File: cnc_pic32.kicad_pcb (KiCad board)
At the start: 4 copper layers, 206.5 x 158.5 mm, 111 parts, among them J1 icd, J13 mrf24j40_tp, J14 mrf24j40_tp, J18 USB_B_Mini, J2 ST7789 oled 128x64, J20 pololu, J21 pololu, J22 pololu, J23 conector oled ST1306 128x32, J24 pololu, J25 pololu, J5 USB_B_Mini, Q1 2N7002, SW2 up, U1 PIC32MX795F512L-80x-PF, U2 FT232BM, U3 LM1117DT-3.3, U4 MRF24J40MA, U5 LM1117DT-3.3, Y2 6MHZ

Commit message: Fix Y1/J17 footprints, update PCB and schematics
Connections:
- U1 pad 21: unconnected-(U1-RB4-Pad21) -> /MCU/RB4
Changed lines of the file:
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@@
 		)
 		(embedded_fonts no)
-		(model "${KICAD6_3DMODEL_DIR}/Resistor_SMD.3dshapes/R_0805_2012Metric.wrl"
+		(model "${KICAD10_3DMODEL_DIR}/Resistor_SMD.3dshapes/R_0805_2012Metric.step"
 			(offset
 				(xyz 0 0 0)
@@
 		)
 		(embedded_fonts no)
-		(model "${KICAD6_3DMODEL_DIR}/Capacitor_SMD.3dshapes/C_0805_2012Metric.wrl"
+		(model "${KICAD10_3DMODEL_DIR}/Capacitor_SMD.3dshapes/C_0805_2012Metric.step"
 			(offset
 				(xyz 0 0 0)
@@
 		)
 		(embedded_fonts no)
-		(model "${KICAD6_3DMODEL_DIR}/Connector_PinHeader_2.54mm.3dshapes/PinHeader_1x06_P2.54mm_Horizontal.wrl"
+		(model "${KICAD10_3DMODEL_DIR}/Connector_PinHeader_2.54mm.3dshapes/PinHeader_1x06_P2.54mm_Horizontal.step"
 			(offset
 				(xyz 0 0 0)
@@
 		)
 		(embedded_fonts no)
-		(model "${KICAD6_3DMODEL_DIR}/Capacitor_SMD.3dshapes/C_0805_2012Metric.wrl"
+		(model "${KICAD10_3DMODEL_DIR}/Capacitor_SMD.3dshapes/C_0805_2012Metric.step"
 			(offset
 				(xyz 0 0 0)
@@
 		)
 		(embedded_fonts no)
-		(model "${KICAD6_3DMODEL_DIR}/Resistor_SMD.3dshapes/R_0805_2012Metric.wrl"
+		(model "${KICAD10_3DMODEL_DIR}/Resistor_SMD.3dshapes/R_0805_2012Metric.step"
 			(offset
 				(xyz 0 0 0)
@@
 		)
 		(embedded_fonts no)
-		(model "${KICAD6_3DMODEL_DIR}/Connector_PinHeader_2.54mm.3dshapes/PinHeader_1x06_P2.54mm_Vertical.wrl"
+		(model "${KICAD10_3DMODEL_DIR}/Connector_PinHeader_2.54mm.3dshapes/PinHeader_1x06_P2.54mm_Vertical.step"
 			(offset
 				(xyz 0 0 0)
@@
 		)
 		(embedded_fonts no)
-		(model "${KICAD6_3DMODEL_DIR}/Capacitor_SMD.3dshapes/C_0805_2012Metric.wrl"
+		(model "${KICAD10_3DMODEL_DIR}/Capacitor_SMD.3dshapes/C_0805_2012Metric.step"
 			(offset
 				(xyz 0 0 0)
@@
 		)
 		(embedded_fonts no)
-		(model "${KICAD6_3DMODEL_DIR}/Resistor_SMD.3dshapes/R_0805_2012Metric.wrl"
+		(model "${KICAD10_3DMODEL_DIR}/Resistor_SMD.3dshapes/R_0805_2012Metric.step"
 			(offset
 				(xyz 0 0 0)
@@
 		)
 		(embedded_fonts no)
-		(model "${KICAD6_3DMODEL_DIR}/Capacitor_SMD.3dshapes/C_0805_2012Metric.wrl"
+		(model "${KICAD10_3DMODEL_DIR}/Capacitor_SMD.3dshapes/C_0805_2012Metric.step"
 			(offset
 				(xyz 0 0 0)
@@
 		)
 		(embedded_fonts no)
-		(model "${KICAD6_3DMODEL_DIR}/Resistor_SMD.3dshapes/R_0805_2012Metric.wrl"
+		(model "${KICAD10_3DMODEL_DIR}/Resistor_SMD.3dshapes/R_0805_2012Metric.step"
 			(offset
 				(xyz 0 0 0)
@@
 		)
 		(embedded_fonts no)
-		(model "${KICAD6_3DMODEL_DIR}/Connector_PinHeader_2.54mm.3dshapes/PinHeader_1x06_P2.54mm_Vertical.wrl"
+		(model "${KICAD10_3DMODEL_DIR}/Connector_PinHeader_2.54mm.3dshapes/PinHeader_1x06_P2.54mm_Vertical.step"
 			(offset
 				(xyz 0 0 0)
@@
 		)
 		(embedded_fonts no)
-		(model "${KICAD6_3DMODEL_DIR}/Connector_PinHeader_2.54mm.3dshapes/PinHeader_1x06_P2.54mm_Vertical.wrl"
+		(model "${KICAD10_3DMODEL_DIR}/Connector_PinHeader_2.54mm.3dshapes/PinHeader_1x06_P2.54mm_Vertical.step"
 			(offset
 				(xyz 0 0 0)
@@
 		)
 		(embedded_fonts no)
-		(model "${KICAD6_3DMODEL_DIR}/Resistor_SMD.3dshapes/R_0805_2012Metric.wrl"
+		(model "${KICAD10_3DMODEL_DIR}/Resistor_SMD.3dshapes/R_0805_2012Metric.step"
 			(offset
 				(xyz 0 0 0)
@@
 		)
 		(embedded_fonts no)
-		(model "${KICAD6_3DMODEL_DIR}/Resistor_SMD.3dshapes/R_0805_2012Metric.wrl"
+		(model "${KICAD10_3DMODEL_DIR}/Resistor_SMD.3dshapes/R_0805_2012Metric.step"
 			(offset
 				(xyz 0 0 0)
@@
 		)
 		(embedded_fonts no)
-		(model "${KICAD6_3DMODEL_DIR}/Resistor_SMD.3dshapes/R_0805_2012Metric.wrl"
+		(model "${KICAD10_3DMODEL_DIR}/Resistor_SMD.3dshapes/R_0805_2012Metric.step"
 			(offset
 				(xyz 0 0 0)
@@
 			)
 		)
-		(attr smd dnp)
+		(attr smd)
 		(duplicate_pad_numbers_are_jumpers no)
 		(fp_line
@@
 		)
 		(embedded_fonts no)
-		(model "${KICAD6_3DMODEL_DIR}/Resistor_SMD.3dshapes/R_0805_2012Metric.wrl"
+		(model "${KICAD10_3DMODEL_DIR}/Resistor_SMD.3dshapes/R_0805_2012Metric.step"
 			(offset
 				(xyz 0 0 0)
@@
 		)
 		(embedded_fonts no)
-		(model "${KICAD6_3DMODEL_DIR}/Display.3dshapes/Adafruit_SSD1306.wrl"
+		(model "${KICAD10_3DMODEL_DIR}/Display.3dshapes/Adafruit_SSD1306.step"
 			(offset
 				(xyz 0 0 0)
@@
 		)
 		(embedded_fonts no)
-		(model "${KICAD6_3DMODEL_DIR}/Resistor_SMD.3dshapes/R_0805_2012Metric.wrl"
+		(model "${KICAD10_3DMODEL_DIR}/Resistor_SMD.3dshapes/R_0805_2012Metric.step"
 			(offset
 				(xyz 0 0 0)
@@
 		)
 		(embedded_fonts no)
-		(model "${KICAD6_3DMODEL_DIR}/Resistor_SMD.3dshapes/R_0805_2012Metric.wrl"
+		(model "${KICAD10_3DMODEL_DIR}/Resistor_SMD.3dshapes/R_0805_2012Metric.step"
 			(offset
 				(xyz 0 0 0)
@@
 		)
 		(embedded_fonts no)
-		(model "${KICAD6_3DMODEL_DIR}/Connector_PinHeader_2.54mm.3dshapes/PinHeader_1x06_P2.54mm_Vertical.wrl"
+		(model "${KICAD10_3DMODEL_DIR}/Connector_PinHeader_2.54mm.3dshapes/PinHeader_1x06_P2.54mm_Vertical.step"
 			(offset
 				(xyz 0 0 0)
@@
 		)
 		(embedded_fonts no)
-		(model "${KICAD6_3DMODEL_DIR}/Capacitor_SMD.3dshapes/C_0805_2012Metric.wrl"
+		(model "${KICAD10_3DMODEL_DIR}/Capacitor_SMD.3dshapes/C_0805_2012Metric.step"
 			(offset
 				(xyz 0 0 0)
@@
 		)
 		(embedded_fonts no)
-		(model "${KICAD6_3DMODEL_DIR}/Resistor_SMD.3dshapes/R_0805_2012Metric.wrl"
+		(model "${KICAD10_3DMODEL_DIR}/Resistor_SMD.3dshapes/R_0805_2012Metric.step"
 			(offset
 				(xyz 0 0 0)
@@
 		)
 		(embedded_fonts no)
-		(model "${KICAD6_3DMODEL_DIR}/Capacitor_SMD.3dshapes/C_0805_2012Metric.wrl"
+		(model "${KICAD10_3DMODEL_DIR}/Capacitor_SMD.3dshapes/C_0805_2012Metric.step"
 			(offset
 				(xyz 0 0 0)
@@
 		)
 		(embedded_fonts no)
-		(model "${KICAD6_3DMODEL_DIR}/Resistor_SMD.3dshapes/R_0805_2012Metric.wrl"
+		(model "${KICAD10_3DMODEL_DIR}/Resistor_SMD.3dshapes/R_0805_2012Metric.step"
 			(offset
 				(xyz 0 0 0)
@@
 		)
 		(embedded_fonts no)
-		(model "${KICAD6_3DMODEL_DIR}/Capacitor_SMD.3dshapes/C_0805_2012Metric.wrl"
+		(model "${KICAD10_3DMODEL_DIR}/Capacitor_SMD.3dshapes/C_0805_2012Metric.step"
 			(offset
 				(xyz 0 0 0)
@@
 		)
 		(embedded_fonts no)
-		(model "${KICAD6_3DMODEL_DIR}/Capacitor_SMD.3dshapes/C_0805_2012Metric.wrl"
+		(model "${KICAD10_3DMODEL_DIR}/Capacitor_SMD.3dshapes/C_0805_2012Metric.step"
 			(offset
 				(xyz 0 0 0)
@@
 		)
 		(embedded_fonts no)
-		(model "${KICAD6_3DMODEL_DIR}/Resistor_SMD.3dshapes/R_0805_2012Metric.wrl"
+		(model "${KICAD10_3DMODEL_DIR}/Resistor_SMD.3dshapes/R_0805_2012Metric.step"
 			(offset
 				(xyz 0 0 0)
@@
 		)
 		(embedded_fonts no)
-		(model "${KICAD6_3DMODEL_DIR}/Resistor_SMD.3dshapes/R_0805_2012Metric.wrl"
+		(model "${KICAD10_3DMODEL_DIR}/Resistor_SMD.3dshapes/R_0805_2012Metric.step"
 			(offset
 				(xyz 0 0 0)
@@
 		)
 		(embedded_fonts no)
-		(model "${KICAD6_3DMODEL_DIR}/Connector_PinHeader_2.54mm.3dshapes/PinHeader_1x06_P2.54mm_Vertical.wrl"
+		(model "${KICAD10_3DMODEL_DIR}/Connector_PinHeader_2.54mm.3dshapes/PinHeader_1x06_P2.54mm_Vertical.step"
 			(offset
 				(xyz 0 0 0)
@@
 					"7" "8" "9" "63" "73" "74" "64" "93" "94" "98" "99" "100" "3" "4" "5"
 					"18" "19" "90" "89" "57" "56" "10" "11" "12" "14" "96" "97" "95" "1"
-					"54" "2" "16" "37" "46" "62" "45" "15" "75" "65" "36" "86" "55" "31"
+					"54" "2" "16" "37" "46" "62" "75" "45" "65" "15" "36" "86" "55" "31"
 					"30" "85" "13" "25" "24" "23" "22" "21" "20" "26" "27" "32" "33" "34"
 					"35" "41" "42" "43" "44" "72" "76" "77" "78" "81" "82" "83" "84" "68"
@@
 			(layers "F.Cu" "F.Mask" "F.Paste")
 			(roundrect_rratio 0.25)
-			(net "unconnected-(U1-RB4-Pad21)")
+			(net "/MCU/RB4")
 			(pinfunction "RB4_21")
 			(pintype "bidirectional")
@@
 		)
 		(embedded_fonts no)
-		(model "${KICAD7_3DMODEL_DIR}/Package_QFP.3dshapes/TQFP-100_14x14mm_P0.5mm.wrl"
+		(model "${KICAD10_3DMODEL_DIR}/Package_QFP.3dshapes/TQFP-100_14x14mm_P0.5mm.step"
 			(offset
 				(xyz 0 0 0)
@@
 		)
 		(embedded_fonts no)
-		(model "${KICAD6_3DMODEL_DIR}/Resistor_SMD.3dshapes/R_0805_2012Metric.wrl"
+		(model "${KICAD10_3DMODEL_DIR}/Resistor_SMD.3dshapes/R_0805_2012Metric.step"
 			(offset
 				(xyz 0 0 0)
@@
 		)
 		(embedded_fonts no)
-		(model "${KICAD6_3DMODEL_DIR}/Resistor_SMD.3dshapes/R_0805_2012Metric.wrl"
+		(model "${KICAD10_3DMODEL_DIR}/Resistor_SMD.3dshapes/R_0805_2012Metric.step"
 			(offset
 				(xyz 0 0 0)
@@
 		)
 		(embedded_fonts no)
-		(model "${KICAD6_3DMODEL_DIR}/Capacitor_SMD.3dshapes/C_0805_2012Metric.wrl"
+		(model "${KICAD10_3DMODEL_DIR}/Capacitor_SMD.3dshapes/C_0805_2012Metric.step"
 			(offset
 				(xyz 0 0 0)
@@
 		(layer "Edge.Cuts")
 	)
-	(group ""
-		(members "2cbcc744-096b-40a3-b78c-918f4a743f47" "2e750bda-fae1-4baf-9608-1bb578c4372c"
-			"6d9d9827-8c7d-4d5b-b699-214eff5a001c" "8ec31916-879c-4656-8221-b70fdec8313c"
-			"940932ac-756b-40a1-9c92-fe3b5d214915" "cddb0360-c104-4524-a5cb-732ba424b167"
-			"e938de00-ce47-48e1-8177-ba1bfbed842c"
-		)
-	)
 	(embedded_fonts no)

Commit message: fix: PCB Edge.Cuts 96x96mm con esquinas redondeadas 5mm
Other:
- board size 206.5 x 158.5 mm -> 96 x 96 mm
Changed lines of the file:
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@@
 	)
 	(gr_line
-		(start 52 26)
-		(end 52 184.5)
+		(start 57 26)
+		(end 143 26)
 		(stroke
 			(width 0.05)
@@
 	)
 	(gr_line
-		(start 52 184.5)
-		(end 258.5 184.5)
+		(start 148 31)
+		(end 148 117)
 		(stroke
 			(width 0.05)
@@
 	)
 	(gr_line
-		(start 258.5 26)
-		(end 52 26)
+		(start 143 122)
+		(end 57 122)
 		(stroke
 			(width 0.05)
@@
 	)
 	(gr_line
-		(start 258.5 184.5)
-		(end 258.5 26)
+		(start 52 117)
+		(end 52 31)
 		(stroke
 			(width 0.05)
+			(type default)
+		)
+		(layer "Edge.Cuts")
+	)
+	(gr_arc
+		(start 57 26)
+		(mid 53.464 27.464)
+		(end 52 31)
+		(stroke
+			(width 0.05)
+			(type default)
+		)
+		(layer "Edge.Cuts")
+	)
+	(gr_arc
+		(start 143 26)
+		(mid 146.536 27.464)
+		(end 148 31)
+		(stroke
+			(width 0.05)
+			(type default)
+		)
+		(layer "Edge.Cuts")
+	)
+	(gr_arc
+		(start 148 117)
+		(mid 146.536 120.536)
+		(end 143 122)
+		(stroke
+			(width 0.05)
+			(type default)
+		)
+		(layer "Edge.Cuts")
+	)
+	(gr_arc
+		(start 57 122)
+		(mid 53.464 120.536)
+		(end 52 117)
+		(stroke
+			(width 0.05)

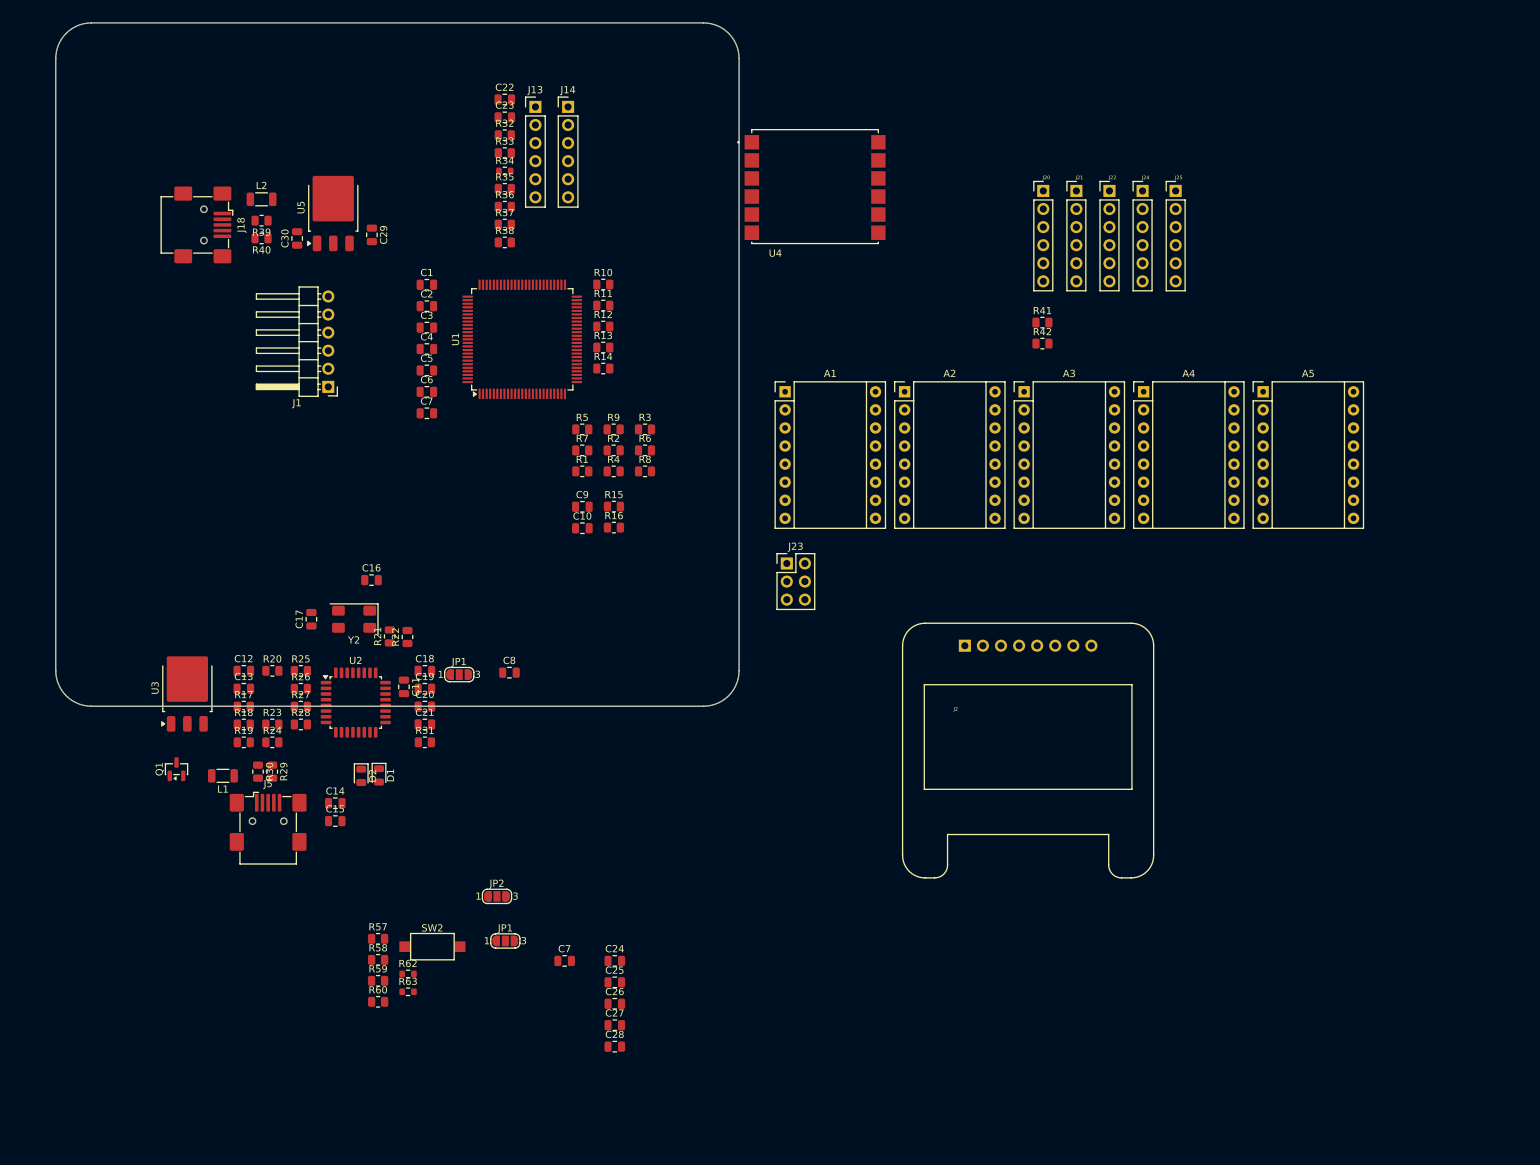
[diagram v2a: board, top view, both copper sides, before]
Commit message: fix: PCB Edge.Cuts 96x96mm rounded corners + reposicionamiento componentes + F.Fab font 0.5mm centrado
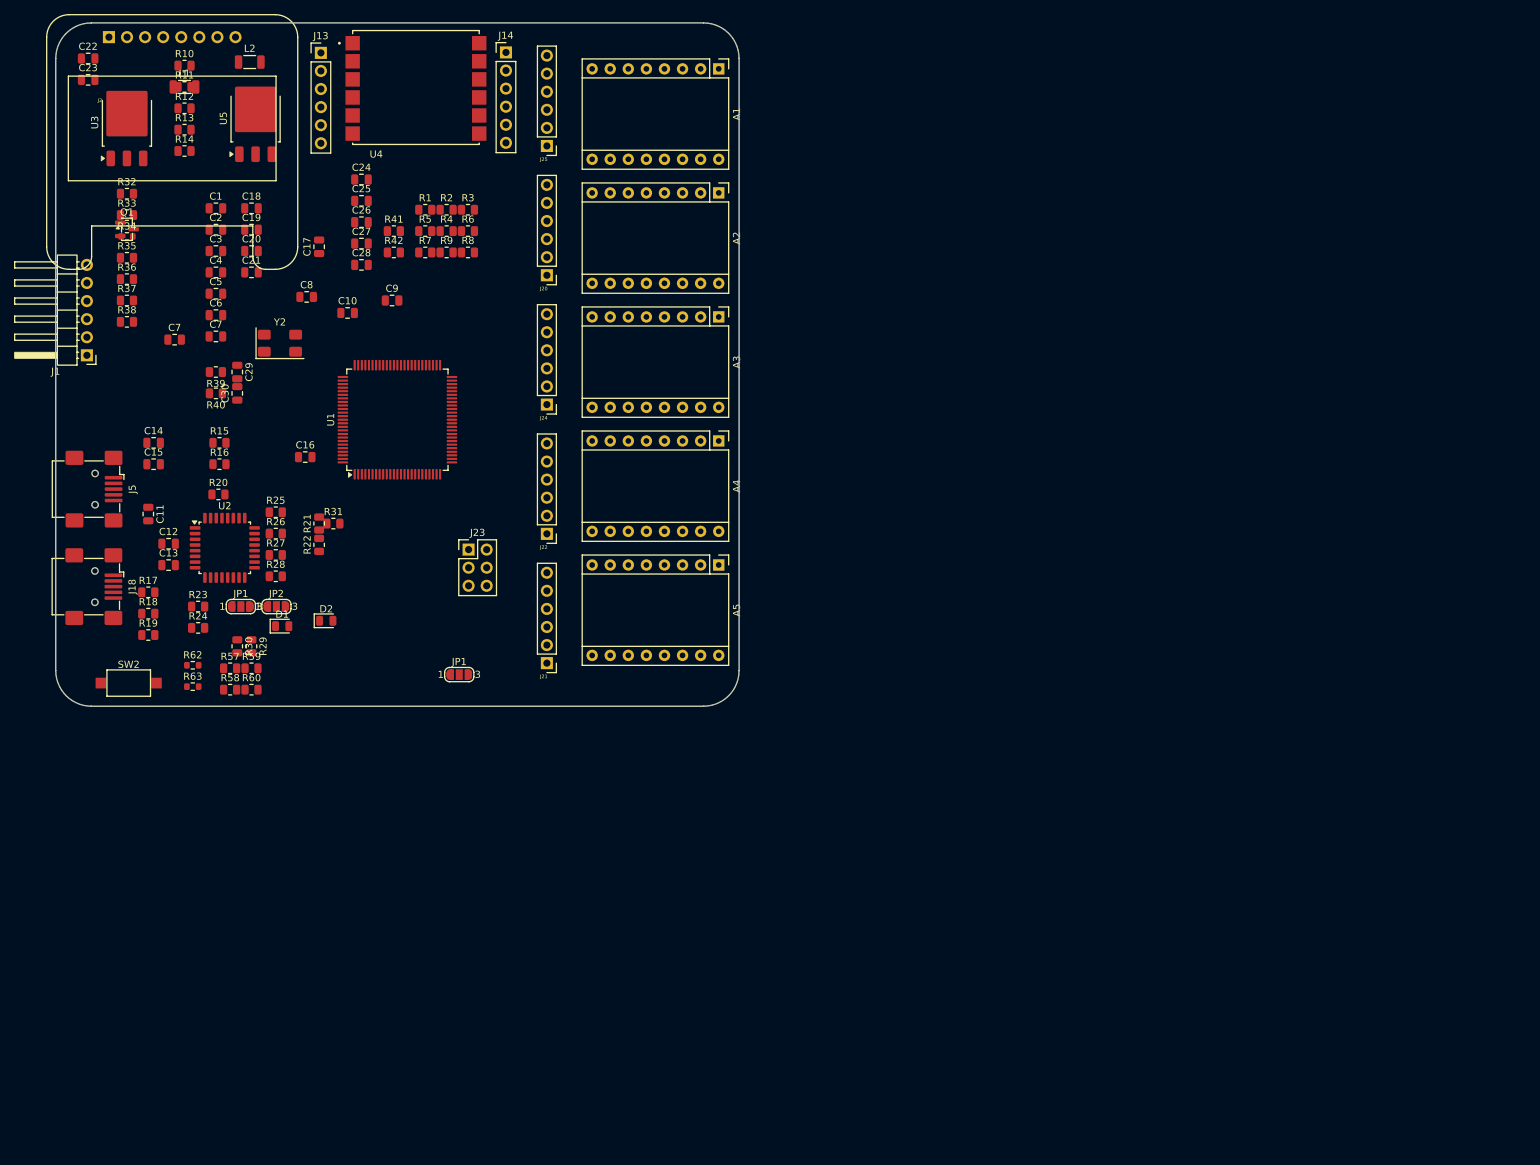
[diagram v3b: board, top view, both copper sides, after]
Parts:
- U4: footprint kiC:MODULE_MRF24J40MA -> Library:MODULE_MRF24J40MA
- moved J2 147.5 mm to (59.5, 28.0)
- moved C28 115.4 mm to (95.0, 60.0)
- moved C27 115.4 mm to (95.0, 57.0)
- moved C26 115.4 mm to (95.0, 54.0)
- moved C25 115.4 mm to (95.0, 51.0)
- moved C24 115.4 mm to (95.0, 48.0)
- moved C7 103.1 mm to (68.7, 70.5)
- moved J21 99.7 mm to (121.0, 116.0), turned to 180 degrees
- moved L1 96.9 mm to (70.1, 35.0), turned to 0 degrees
- moved J22 92.6 mm to (121.0, 97.8), turned to 180 degrees
- moved R41 92.0 mm to (99.5, 55.2)
- moved R42 92.0 mm to (99.5, 58.2)
- moved J24 88.9 mm to (121.0, 79.6), turned to 180 degrees
- moved J25 88.6 mm to (121.0, 43.3), turned to 180 degrees
- moved A5 80.3 mm to (145.1, 102.2), turned to -90 degrees
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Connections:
- R57 pad 2: Net-(R57-Pad2) -> /MCU/RD5
- R58 pad 2: Net-(R58-Pad2) -> /MCU/RD4
- R62 pad 2: Net-(R62-Pad2) -> /MCU/RD7
- R63 pad 2: Net-(R63-Pad2) -> /MCU/RD6
- SW2 pad 1: Net-(R58-Pad2) -> /MCU/RD4
